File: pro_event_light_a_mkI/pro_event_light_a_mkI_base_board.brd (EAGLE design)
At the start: 107.7 x 88.4 mm, 93 parts, among them K1 62201021121, SW1 ALPS_EC11D

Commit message: first push to remote repository
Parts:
- moved R6 45.8 mm to (79.5, 81.9), turned to 90 degrees
- moved LEDR1 40.9 mm to (68.1, 75.9), turned to 90 degrees
- moved LEDB2 40.3 mm to (62.7, 57.8), turned to 90 degrees
- moved LEDB1 38.3 mm to (62.7, 68.5), turned to 90 degrees
- moved LEDG1 35.2 mm to (75.9, 75.2), turned to 0 degrees
- moved R1 34.0 mm to (89.2, 76.2), turned to 90 degrees
- moved LEDR3 33.7 mm to (85.3, 75.8), turned to 90 degrees
- moved LEDR5 31.2 mm to (68.1, 54.6), turned to 90 degrees
- moved LEDR2 27.2 mm to (68.1, 65.2), turned to 90 degrees
- moved LEDG2 24.6 mm to (75.9, 69.3), turned to 0 degrees
- moved LEDB4 23.7 mm to (90.6, 58.2)
- moved LEDB3 23.3 mm to (90.7, 68.7)
- moved LEDW2 17.7 mm to (75.8, 65.2), turned to 180 degrees
- moved R4 15.8 mm to (73.0, 55.1), turned to 0 degrees
- moved LEDR6 15.4 mm to (85.2, 54.6), turned to 90 degrees
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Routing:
- net DRIVER_LEDB: track 80.2 -> 13.4 mm
- net DRIVER_LEDR: track 36.5 -> 13.4 mm
- net N$14: track 33.4 -> 13.4 mm
- net VSENSE_LEDR: track 76.6 -> 90.6 mm
- net VSENSE_LEDB: track 75.2 -> 62.0 mm
- net N$6: track 29.6 -> 18.2 mm
- net N$4: track 24.8 -> 18.3 mm
- net N$3: track 12.8 -> 16.9 mm
- net N$25: track 12.3 -> 16.2 mm
- net VSENSE_LEDG: track 9.22 -> 11.1 mm

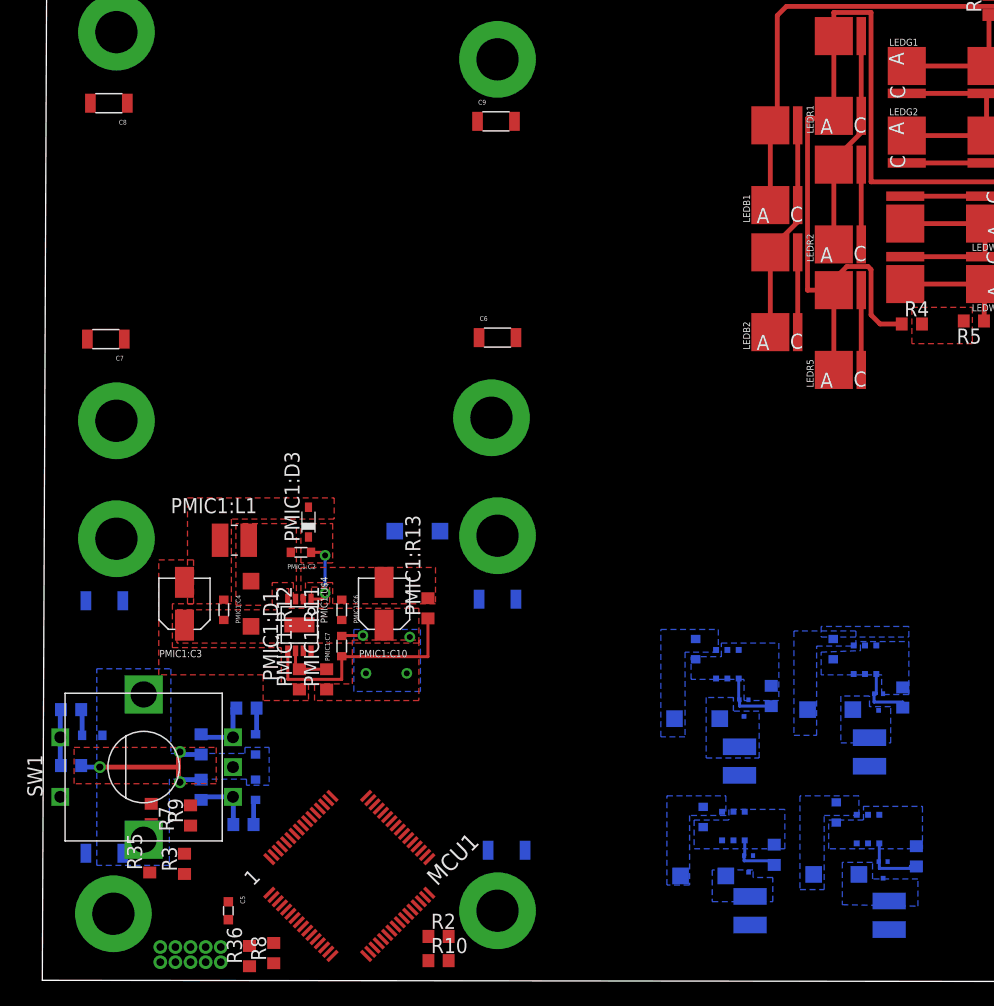
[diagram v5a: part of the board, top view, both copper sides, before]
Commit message: saving an intermediate 'snapshot' -> maybe we have to revert afterwards. This layout will take all Infineon chips on the 'power' board
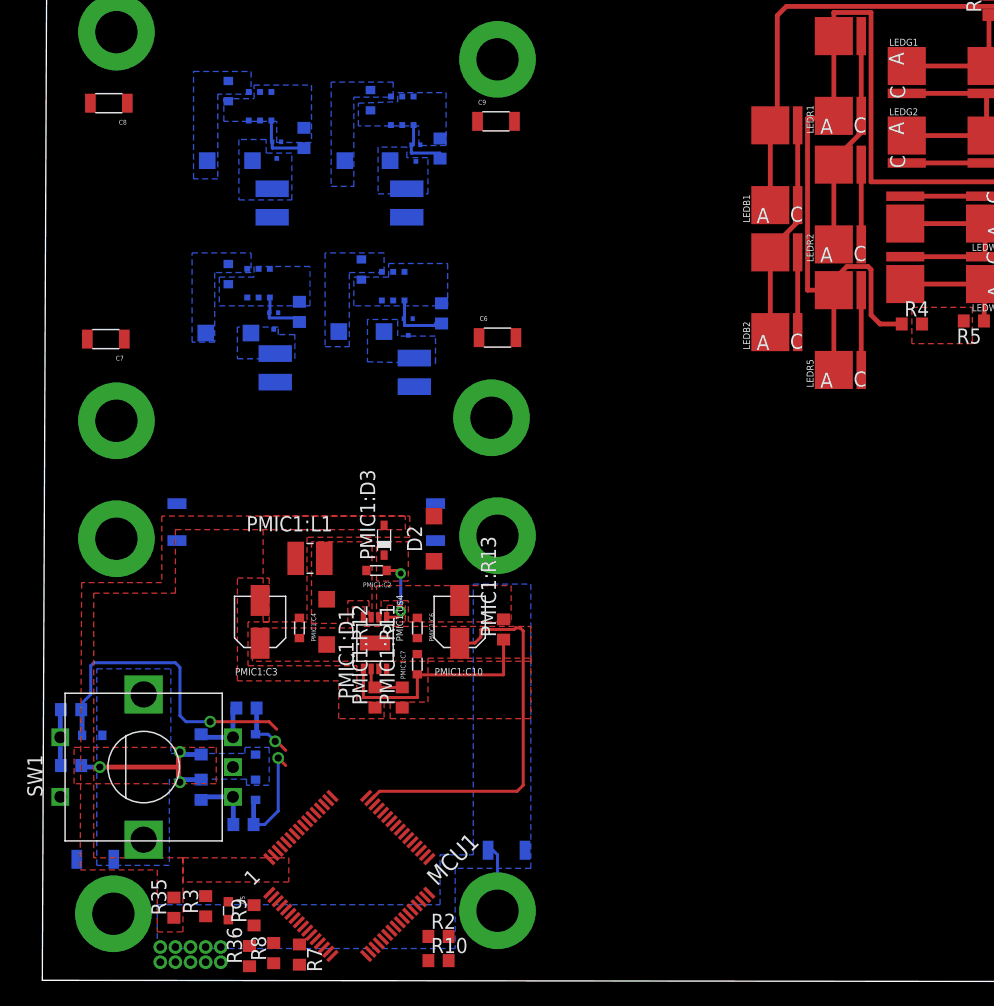
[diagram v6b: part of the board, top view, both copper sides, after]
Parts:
- moved PMIC3:L2 61.1 mm to (19.3, 65.3)
- moved PMIC3:PMIC1 61.1 mm to (18.3, 73.4)
- moved PMIC3:C8 61.1 mm to (15.6, 74.7)
- moved PMIC3:DZ1 61.1 mm to (15.7, 68.8)
- moved PMIC3:R14 61.1 mm to (22.0, 70.7)
- moved PMIC3:U1 61.1 mm to (19.7, 69.7)
- moved PMIC4:C8 60.6 mm to (26.8, 59.7)
- moved PMIC4:DZ1 60.6 mm to (26.8, 54.5)
- moved PMIC4:L2 60.6 mm to (31.2, 51.1)
- moved PMIC4:PMIC1 60.6 mm to (29.5, 58.3)
- moved PMIC4:R14 60.6 mm to (33.5, 56.0)
- moved PMIC5:C8 60.6 mm to (15.6, 59.3)
- moved PMIC5:DZ1 60.6 mm to (15.6, 54.4)
- moved PMIC5:L2 60.6 mm to (19.6, 51.4)
- moved PMIC5:PMIC1 60.6 mm to (18.2, 58.5)
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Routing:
- net GND_MCU: track 1.31 -> 32.7 mm, vias 4 -> 0
- net ENCODER_D: track 2.24 -> 28.8 mm, vias 0 -> 1
- net ENCODER_A: track 2.24 -> 10.1 mm, vias 0 -> 1
- net N$9: track 0.00 -> 5.64 mm
- net ENCODER_B: track 2.29 -> 5.30 mm, vias 0 -> 1
- added copper zone on layer 16, net N$13

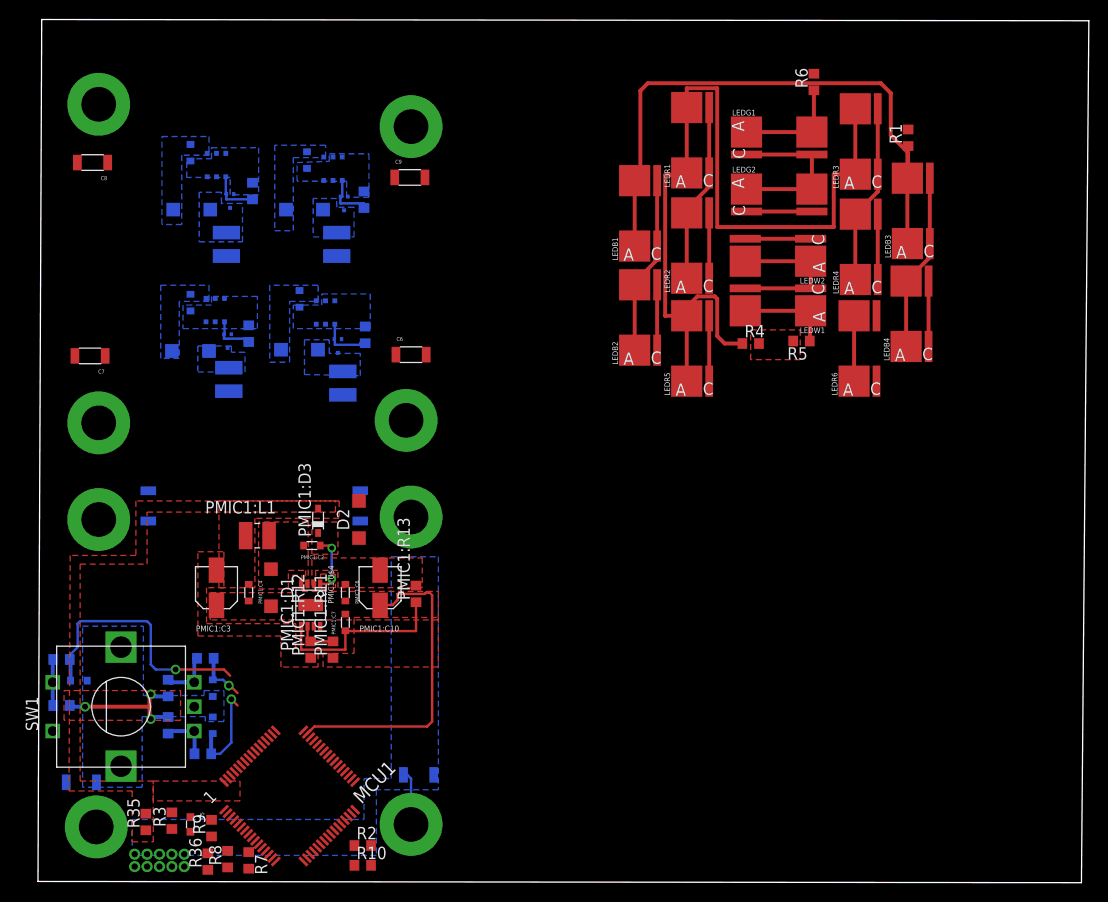
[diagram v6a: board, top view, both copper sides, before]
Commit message: final commit for today. LEDs are rearranged, looks pretty good right now
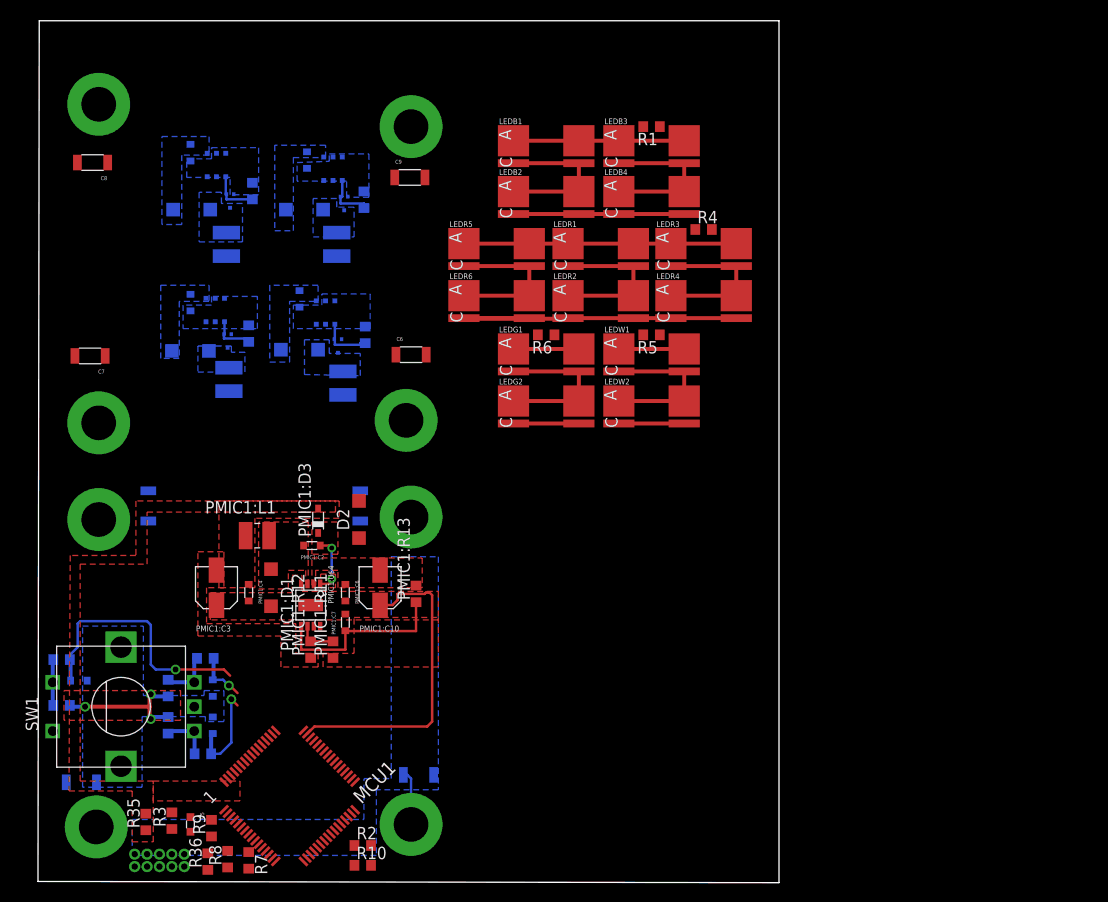
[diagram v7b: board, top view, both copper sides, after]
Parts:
- moved LEDR6 38.4 mm to (47.0, 58.4), turned to 0 degrees
- moved R6 37.7 mm to (52.1, 56.0), turned to 180 degrees
- moved LEDG1 32.6 mm to (52.1, 53.0)
- moved LEDG2 32.3 mm to (52.1, 47.6)
- moved LEDB4 29.8 mm to (62.9, 69.1), turned to 0 degrees
- moved LEDB3 28.4 mm to (62.9, 74.3), turned to 0 degrees
- moved R1 26.3 mm to (62.9, 77.3), turned to 180 degrees
- moved LEDR5 23.0 mm to (47.0, 63.8), turned to 0 degrees
- moved LEDW2 21.8 mm to (62.9, 47.6), turned to 0 degrees
- moved LEDR3 21.0 mm to (68.2, 63.8), turned to 0 degrees
- moved LEDR4 18.4 mm to (68.2, 58.4), turned to 0 degrees
- moved LEDR1 16.0 mm to (57.7, 63.8), turned to 0 degrees
- moved LEDB2 15.5 mm to (52.1, 69.1), turned to 0 degrees
- moved R5 15.4 mm to (62.9, 56.0)
- moved LEDW1 14.8 mm to (62.9, 53.0), turned to 0 degrees
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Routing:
- net VSENSE_LEDR: track 90.6 -> 27.9 mm
- net VSENSE_LEDB: track 62.0 -> 17.5 mm
- net DRIVER_LEDR: track 13.4 -> 35.9 mm
- net VSENSE_LEDG: track 11.1 -> 6.70 mm
- net DRIVER_LEDB: track 13.4 -> 17.5 mm
- net VSENSE_LEDW: track 9.80 -> 6.70 mm
- net N$14: track 13.4 -> 16.4 mm
- net N$7: track 18.4 -> 16.4 mm
- net N$4: track 18.3 -> 16.3 mm
- net N$12: track 18.4 -> 16.4 mm
- net N$6: track 18.2 -> 16.3 mm
- net N$3: track 16.9 -> 16.4 mm
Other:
- board size 107.7 x 88.4 mm -> 75.9 x 88.3 mm
